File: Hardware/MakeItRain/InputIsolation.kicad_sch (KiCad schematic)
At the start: 21 parts, among them IC2 LTV-846S, Q14 BS250, Q15 BS250, Q16 BS250, Q17 BS250

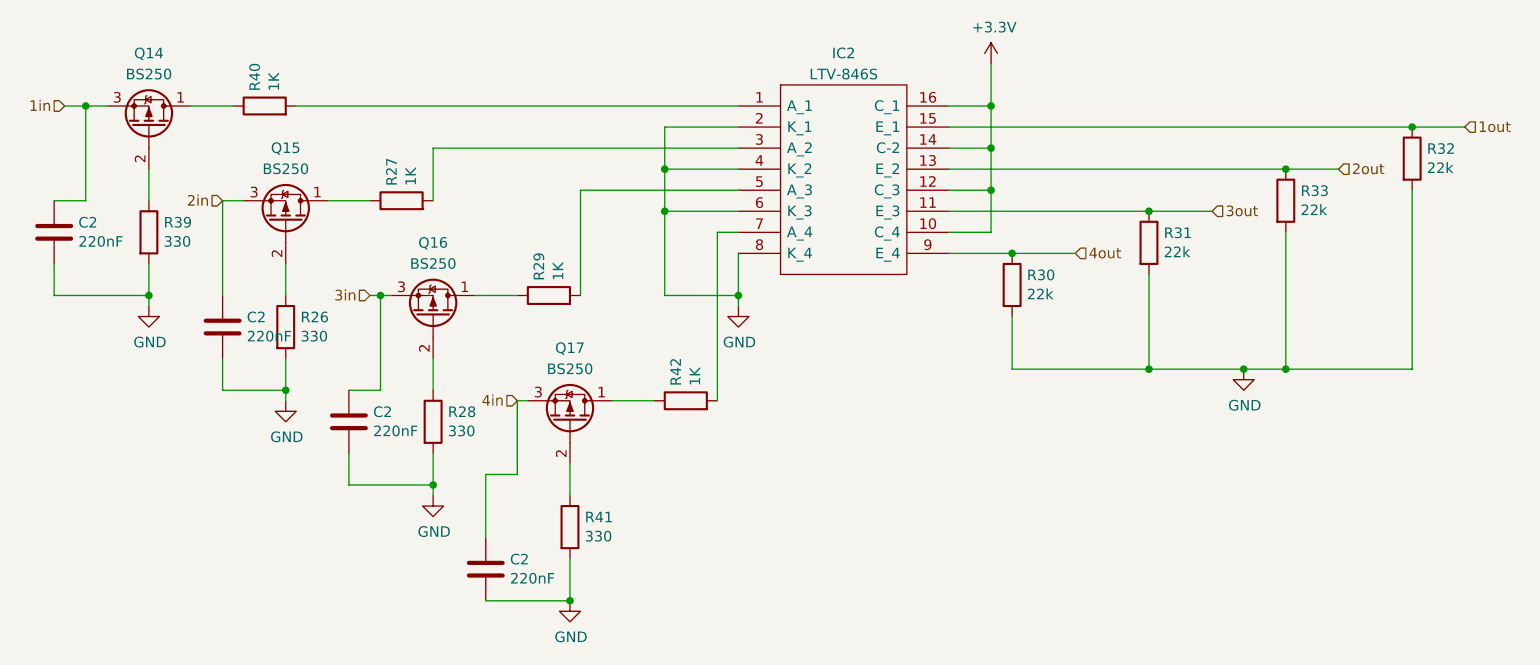
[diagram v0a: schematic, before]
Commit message: wip for adding RTC
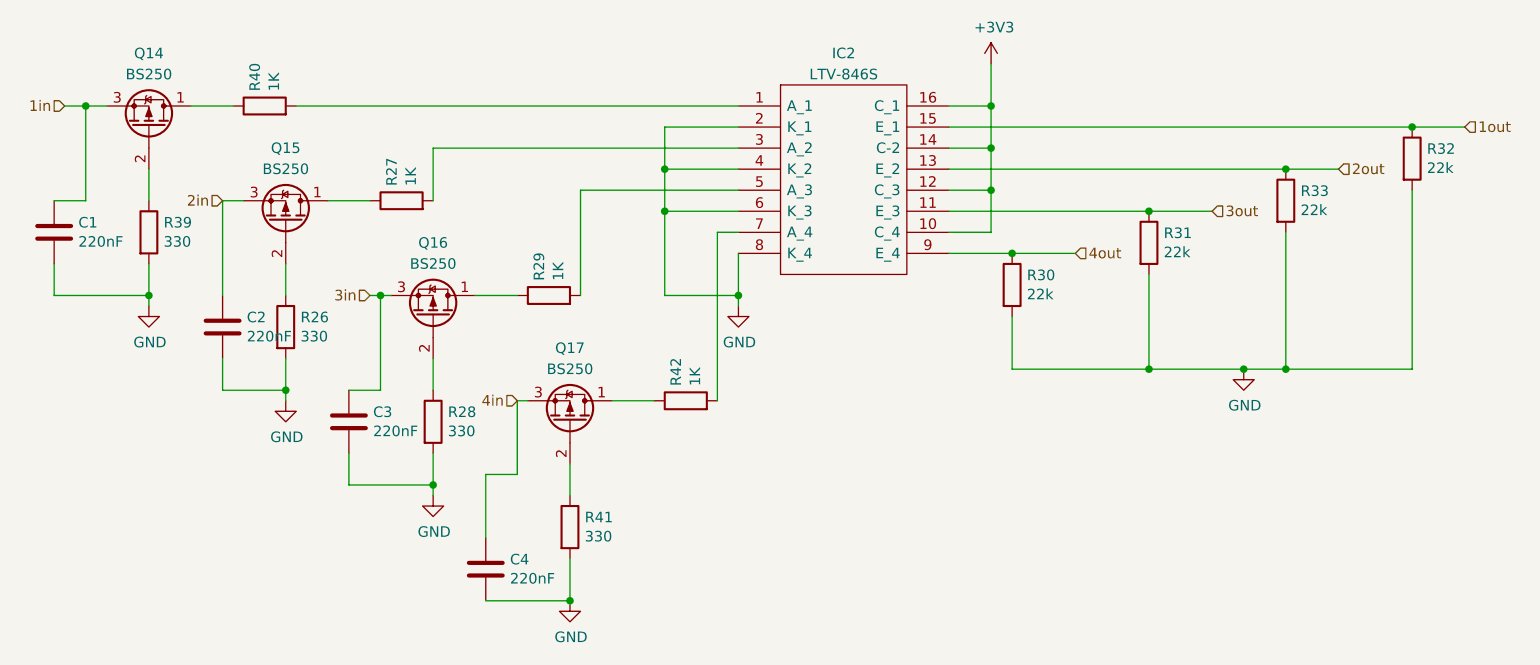
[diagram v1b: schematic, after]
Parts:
- renumbered C2 to C1, C2 to C3, C2 to C4

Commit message: wip
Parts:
- R26, R27, R28, R29, R30, R31, R32, R33, R39, R40, R41, R42: footprint Resistor_THT:R_Axial_DIN0207_L6.3mm_D2.5mm_P2.54mm_Vertical -> Resistor_SMD:R_1206_3216Metric_Pad1.30x1.75mm_HandSolder
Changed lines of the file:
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@@
 			)
 		)
-		(property "Footprint" "Resistor_THT:R_Axial_DIN0207_L6.3mm_D2.5mm_P2.54mm_Vertical"
+		(property "Footprint" "Resistor_SMD:R_1206_3216Metric_Pad1.30x1.75mm_HandSolder"
 			(at 202.692 67.31 90)
 			(effects
@@
 			)
 		)
-		(property "Footprint" "Resistor_THT:R_Axial_DIN0207_L6.3mm_D2.5mm_P2.54mm_Vertical"
+		(property "Footprint" "Resistor_SMD:R_1206_3216Metric_Pad1.30x1.75mm_HandSolder"
 			(at 82.55 74.168 90)
 			(effects
@@
 			)
 		)
-		(property "Footprint" "Resistor_THT:R_Axial_DIN0207_L6.3mm_D2.5mm_P2.54mm_Vertical"
+		(property "Footprint" "Resistor_SMD:R_1206_3216Metric_Pad1.30x1.75mm_HandSolder"
 			(at 170.942 77.47 90)
 			(effects
@@
 			)
 		)
-		(property "Footprint" "Resistor_THT:R_Axial_DIN0207_L6.3mm_D2.5mm_P2.54mm_Vertical"
+		(property "Footprint" "Resistor_SMD:R_1206_3216Metric_Pad1.30x1.75mm_HandSolder"
 			(at 101.092 111.76 90)
 			(effects
@@
 			)
 		)
-		(property "Footprint" "Resistor_THT:R_Axial_DIN0207_L6.3mm_D2.5mm_P2.54mm_Vertical"
+		(property "Footprint" "Resistor_SMD:R_1206_3216Metric_Pad1.30x1.75mm_HandSolder"
 			(at 116.84 98.298 90)
 			(effects
@@
 			)
 		)
-		(property "Footprint" "Resistor_THT:R_Axial_DIN0207_L6.3mm_D2.5mm_P2.54mm_Vertical"
+		(property "Footprint" "Resistor_SMD:R_1206_3216Metric_Pad1.30x1.75mm_HandSolder"
 			(at 66.802 87.63 90)
 			(effects
@@
 			)
 		)
-		(property "Footprint" "Resistor_THT:R_Axial_DIN0207_L6.3mm_D2.5mm_P2.54mm_Vertical"
+		(property "Footprint" "Resistor_SMD:R_1206_3216Metric_Pad1.30x1.75mm_HandSolder"
 			(at 66.04 62.738 90)
 			(effects
@@
 			)
 		)
-		(property "Footprint" "Resistor_THT:R_Axial_DIN0207_L6.3mm_D2.5mm_P2.54mm_Vertical"
+		(property "Footprint" "Resistor_SMD:R_1206_3216Metric_Pad1.30x1.75mm_HandSolder"
 			(at 187.452 72.39 90)
 			(effects
@@
 			)
 		)
-		(property "Footprint" "Resistor_THT:R_Axial_DIN0207_L6.3mm_D2.5mm_P2.54mm_Vertical"
+		(property "Footprint" "Resistor_SMD:R_1206_3216Metric_Pad1.30x1.75mm_HandSolder"
 			(at 50.292 76.2 90)
 			(effects
@@
 			)
 		)
-		(property "Footprint" "Resistor_THT:R_Axial_DIN0207_L6.3mm_D2.5mm_P2.54mm_Vertical"
+		(property "Footprint" "Resistor_SMD:R_1206_3216Metric_Pad1.30x1.75mm_HandSolder"
 			(at 100.33 85.598 90)
 			(effects
@@
 			)
 		)
-		(property "Footprint" "Resistor_THT:R_Axial_DIN0207_L6.3mm_D2.5mm_P2.54mm_Vertical"
+		(property "Footprint" "Resistor_SMD:R_1206_3216Metric_Pad1.30x1.75mm_HandSolder"
 			(at 84.582 99.06 90)
 			(effects
@@
 			)
 		)
-		(property "Footprint" "Resistor_THT:R_Axial_DIN0207_L6.3mm_D2.5mm_P2.54mm_Vertical"
+		(property "Footprint" "Resistor_SMD:R_1206_3216Metric_Pad1.30x1.75mm_HandSolder"
 			(at 154.432 82.55 90)
 			(effects
